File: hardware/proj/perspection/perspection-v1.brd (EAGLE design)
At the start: 90 x 70 mm, 270 parts, among them J1 MICRO-USB-10118192-0001LF, J10 1X5, J2 1X6-PTSA_1.5/6-3.5-Z, J3 1X2-PTSA_1.5/2-3.5-Z, J4 1X2-JST-PH-SMD, J5 1X2-0428202213, J6 JTAG-ARM_TC-10, J7 JTAG-ARM_TC-10, J8 1X3-0.1IN_THRUHOLE, J9 1X2-PTSA_1.5/2-3.5-Z, Q1 NMOS-CSD18533Q5A, Q10 NMOS-CSD18533Q5A, Q11 IRFML8244TRPBF, Q2 NMOS-CSD18533Q5A, Q3 NMOS-CSD18533Q5A, Q4 NMOS-CSD18533Q5A, Q5 NMOS-CSD18533Q5A, Q6 NMOS-CSD18533Q5A, Q7 NMOS-CSD18533Q5A, Q8 BSS138L, Q9 BSS138L, U1 ATUM, U10 DRV8301DCAR, U11 OPA2374AIDCNR, U12 OPA170AIDBVR, U13 BNO055, U14 TPS81256, U2 FT232RQ, U3 TPS79933DDCR, U4 MCP73831T-2ACI/OT, U5 TMS320F28069MPZT, U6 DRV8801PWPR, U7 DRV8801PWPR, U8 DRV8801PWPR, U9 DRV8801PWPR, Y1 32.768kHz

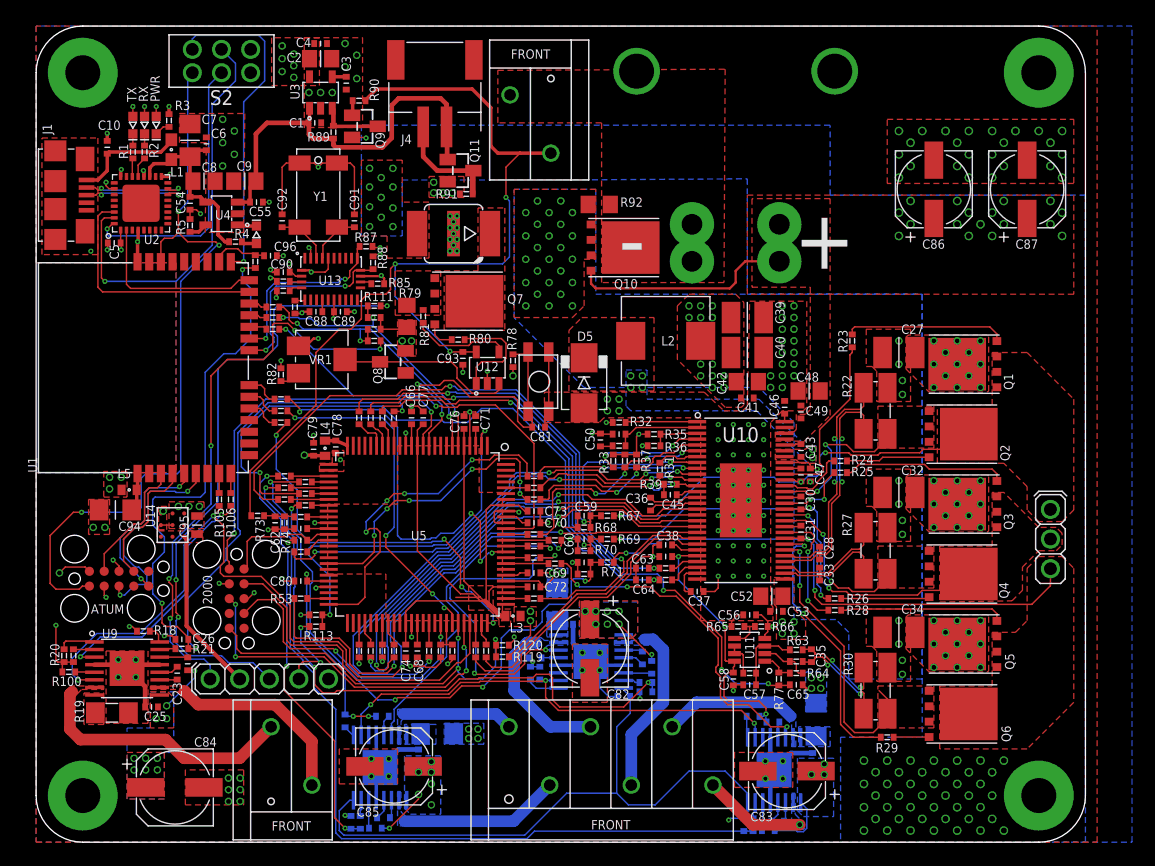
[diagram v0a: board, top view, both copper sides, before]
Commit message: added 4 pin connector, cleaned up test layer, added block diagram, changed GVDD cap to a larger package for higher voltage rating, removed unused cam files, added our own cam processor, added LED_PWM to atum
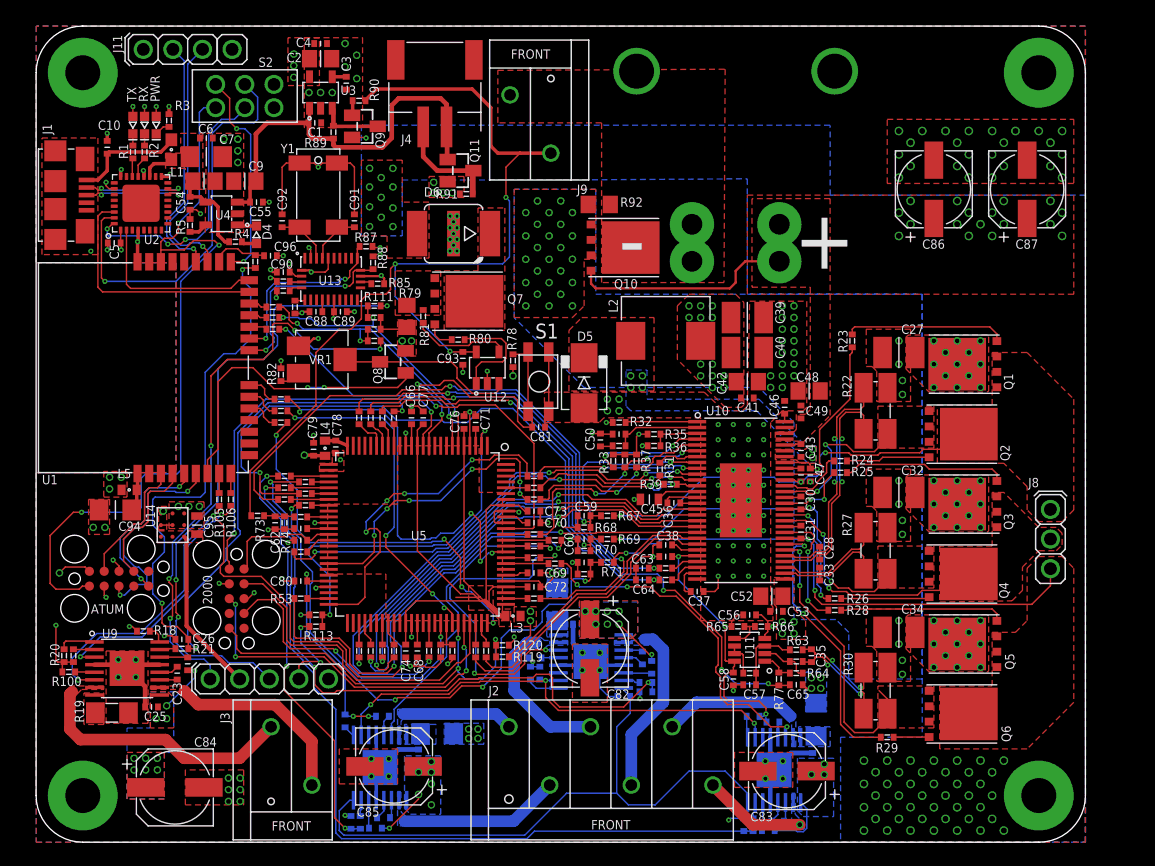
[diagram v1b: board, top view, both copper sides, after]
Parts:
- added J11: 1X4, perspection:1X4_0.1IN_THRUHOLE
- C45: device perspection:C0402 -> perspection:C0603
- moved S2 3.61 mm to (17.9, 64.0)
- moved C36 2.00 mm to (54.7, 29.1), turned to 0 degrees
- moved C7 1.98 mm to (14.6, 58.8), turned to 0 degrees
- moved C45 1.84 mm to (52.6, 29.4)
- moved C6 0.50 mm to (14.6, 60.4), turned to 0 degrees
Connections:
- removed net ATUM_B5: U1.7
- net +3V3: now also J11.1
- net ATUM_ADC4: now also J11.3
- net ATUM_ADC5: now also J11.2
- net GND: now also J11.4
- net LED_PWM: now also U1.7
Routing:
- net LED_PWM: track 0.00 -> 26.5 mm, vias 0 -> 2
- net ATUM_ADC4: track 0.00 -> 21.9 mm, vias 0 -> 1
- net ATUM_ADC5: track 0.00 -> 21.0 mm, vias 0 -> 1
- net BOOTLOADER_CTRL: track 28.2 -> 18.2 mm, vias 1 -> 2
- net +5V: track 16.2 -> 11.8 mm
- net N$42: track 4.26 -> 1.46 mm
- net GVDD: track 1.86 -> 3.60 mm
- net N$41: track 4.30 -> 2.97 mm
- net !RTS_FTDI: track 24.1 -> 23.1 mm, vias 1 -> 3
- net !DTR_FTDI: track 35.1 -> 34.5 mm
- net +3V3: vias 50 -> 47
- added copper zone on layer 1, net +5V

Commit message: ORDER THIS SHIT
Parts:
- added R124, R125, R126: 0, perspection:R0402
- R119, R121: value (none) -> 820
- R120, R122: value (none) -> 2.2k
- moved R17 2.25 mm to (59.4, 10.0), turned to 90 degrees
- moved R98 0.71 mm to (63.7, 10.8)
- moved R13 0.10 mm to (42.3, 14.5)
- moved R7 0.10 mm to (43.1, 14.5)
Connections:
- removed net ATUM_ADC6: U1.28
- removed net ATUM_ADC7: U1.29
- new net N$50: R126.1, U5.40
- new net _PHASE1: R124.1, U5.48
- new net _PHASE2: R125.1, U5.42
- net PHASE1: now also R124.2
- net PHASE2: now also R125.2
- net PHASE3: now also R126.2
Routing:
- net N$50: track 0.00 -> 42.9 mm, vias 0 -> 4
- net PHASE2: track 0.00 -> 38.5 mm, vias 0 -> 3
- net _PHASE1: track 0.00 -> 15.2 mm, vias 0 -> 2
- net PHASE3: track 0.00 -> 7.16 mm, vias 0 -> 1
- net PHASE1: track 0.00 -> 5.88 mm, vias 0 -> 1
- net +3V3: track 82.1 -> 85.9 mm
- net ENABLE2: track 29.0 -> 25.4 mm
- net N$51: track 76.7 -> 74.6 mm
- net _PHASE2: track 0.00 -> 2.10 mm
- net ENABLE1: track 26.9 -> 25.8 mm
- net _SPI_SCK: track 34.6 -> 35.4 mm
- net VC_FB: track 48.5 -> 49.3 mm
- net !SLEEP3: track 1.35 -> 2.06 mm
- net ENABLE3: track 29.7 -> 30.3 mm
- net VPROPI3: vias 1 -> 3
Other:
- board text added: "+3V3"
- board text added: "A4"
- board text added: "A5"
- board text added: "DEBUG"
- board text added: "GND"
- board text added: "PICCOLO"
- board text added: "PROG"
- board text removed: "2000"

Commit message: no board changes. gave every net a class related to its voltage, and created a script to assign a voltage attribute to every capacitor.
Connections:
- net N$13 renamed CP2_M1
- net N$14 renamed CP1_M1
- net N$18 renamed CP2_M2
- net N$19 renamed CP1_M2
- net N$22 renamed CP2_M3
- net N$23 renamed CP1_M3
- net N$28 renamed CP2_MAUX
- net N$29 renamed CP1_MAUX
